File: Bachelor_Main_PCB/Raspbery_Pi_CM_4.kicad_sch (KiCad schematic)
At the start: 10 parts, among them J21 M20-9990245, Q12 NX3008NBKW, Q2 SSM3J358R,LF, U1 SC0683, X1 DF40HC_3.0_-100DS-0.4V_58, X2 DF40HC_3.0_-100DS-0.4V_58

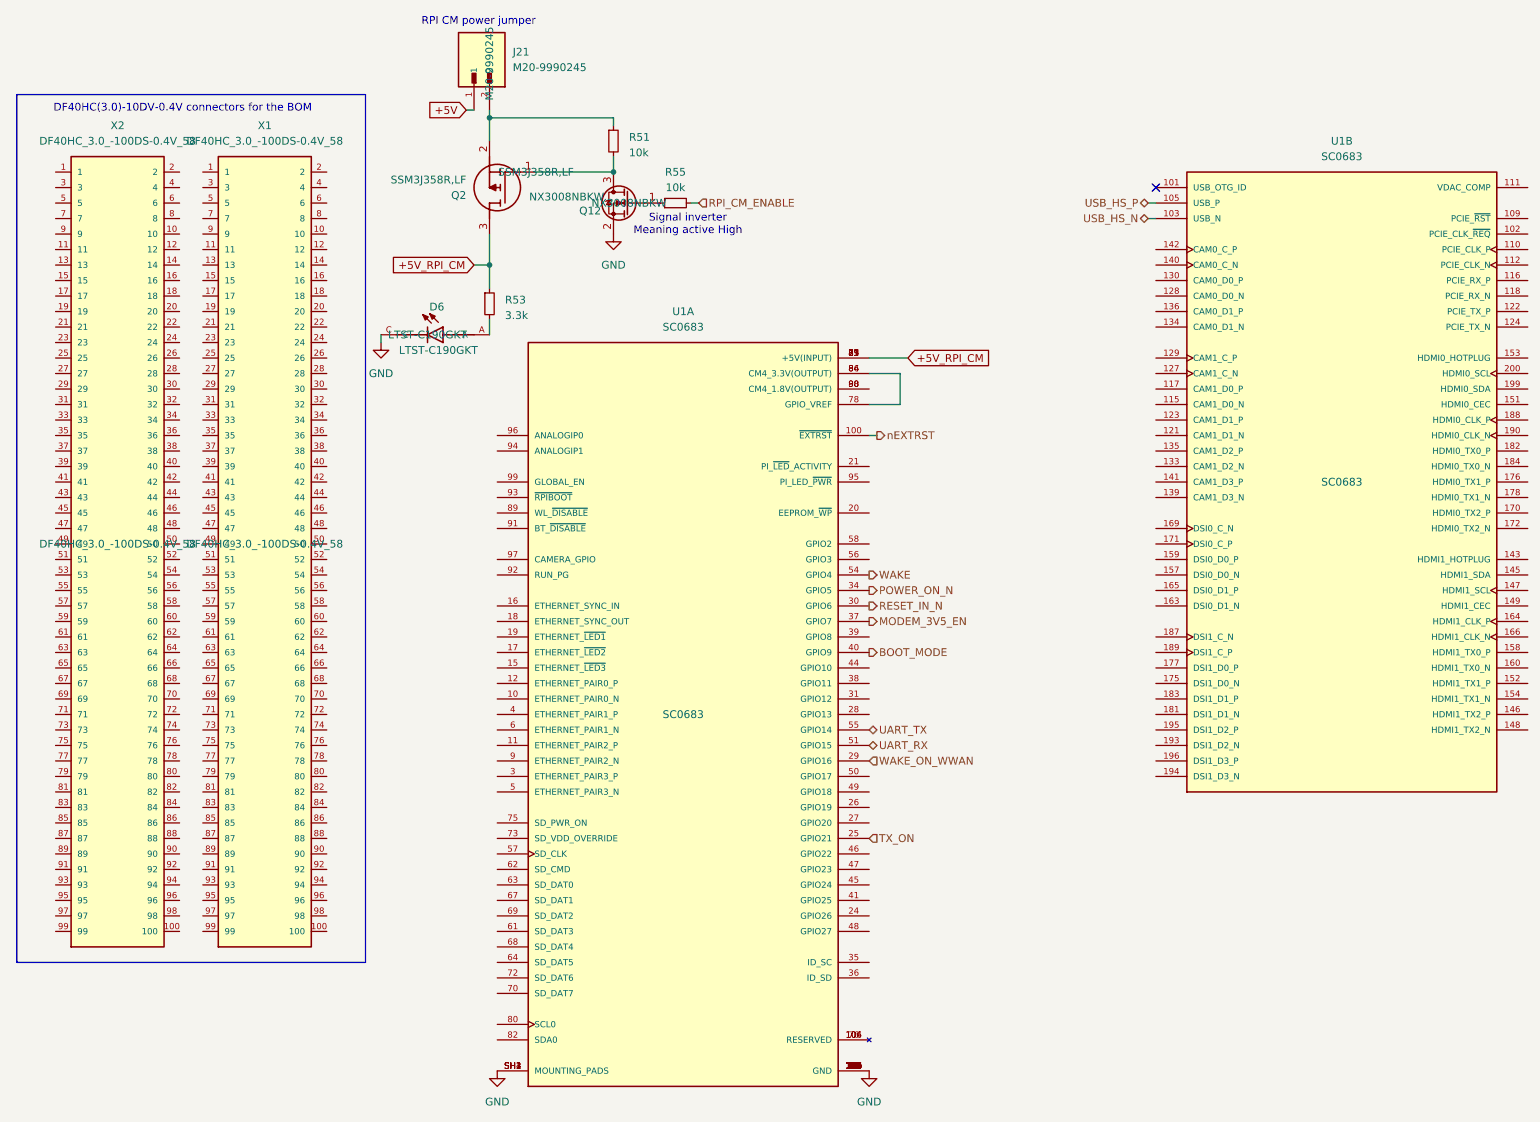
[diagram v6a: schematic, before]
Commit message: Add 1% tolerance field to high tolerance resistors
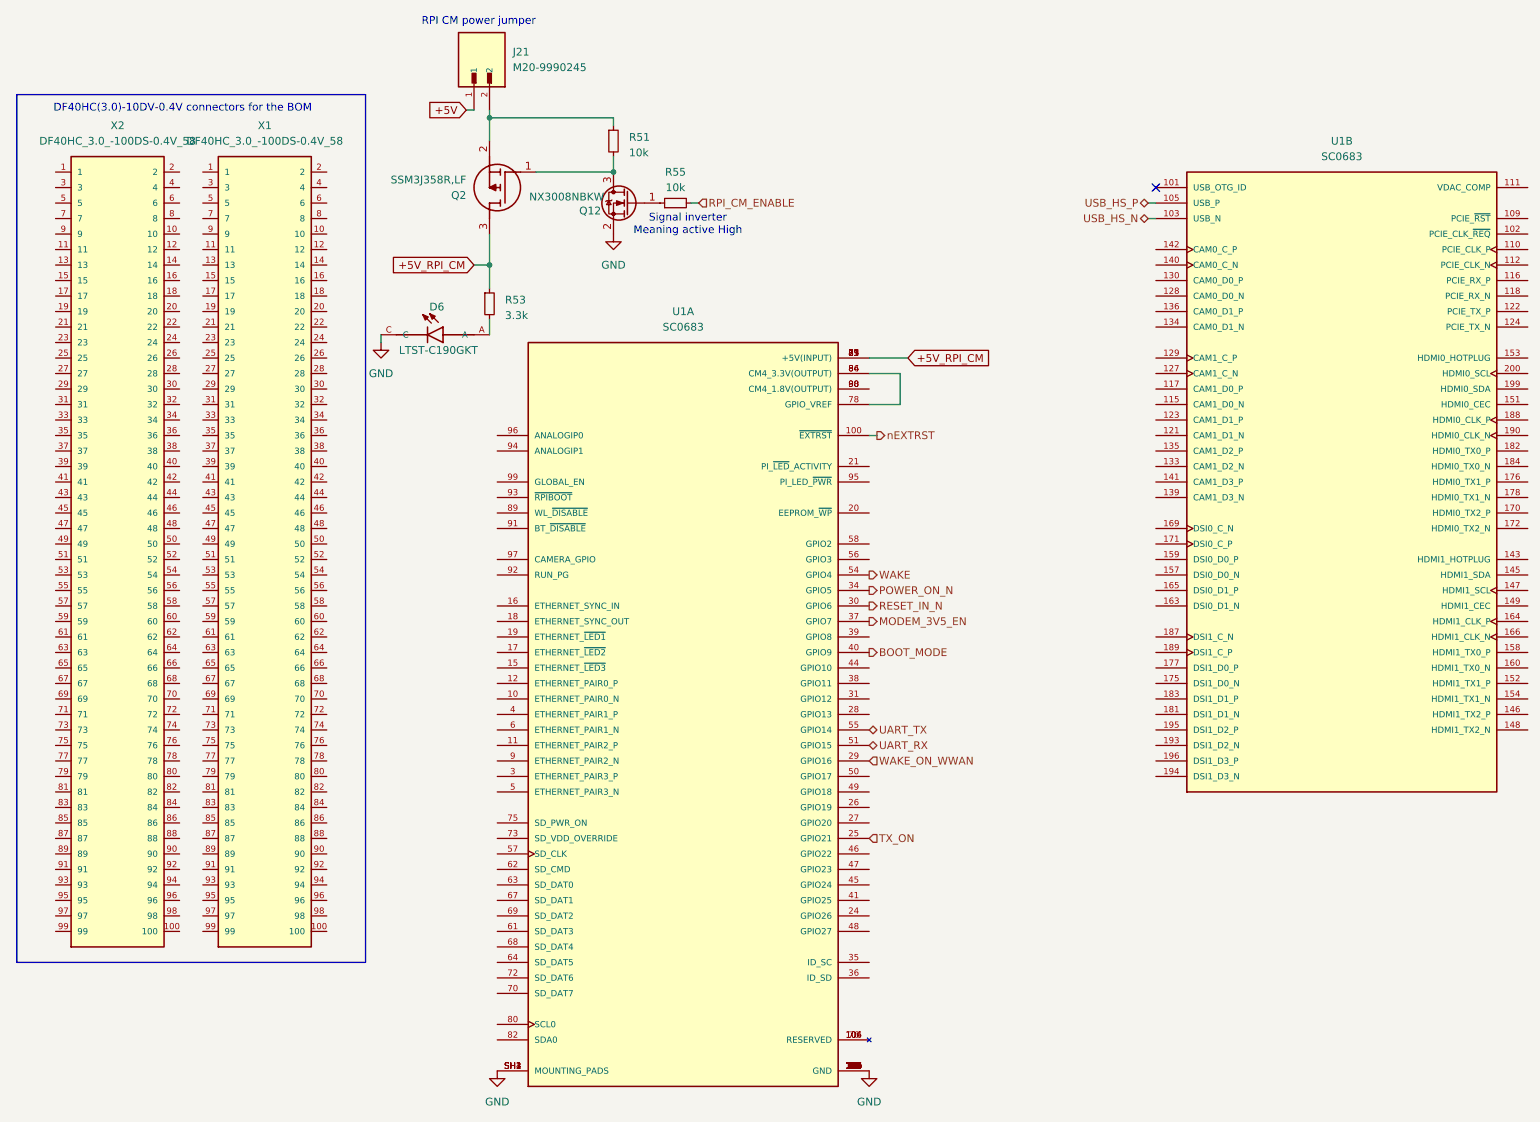
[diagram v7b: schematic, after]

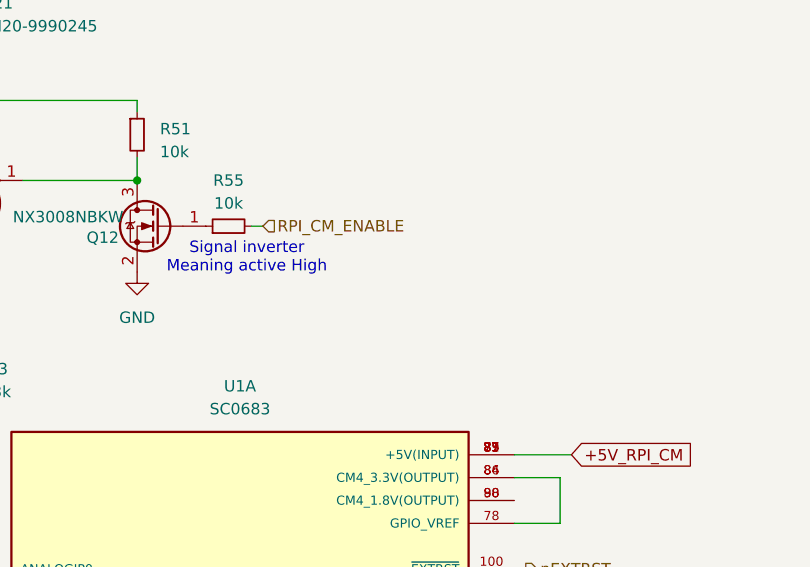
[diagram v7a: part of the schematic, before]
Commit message: Add pulldown to power switch mosfets
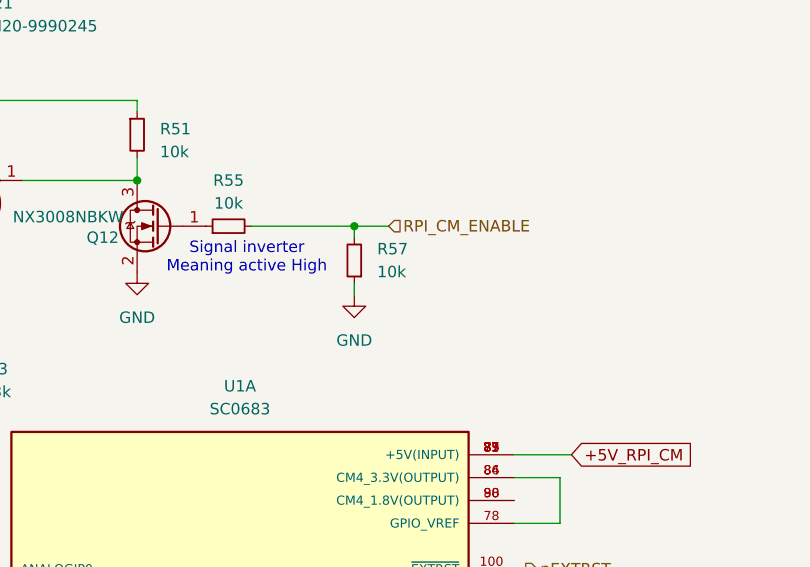
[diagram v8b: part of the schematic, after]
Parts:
- added R57: 10k, Resistor_SMD:R_0603_1608Metric, symbol Device:R_Small
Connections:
- net GND: now also R57.1
- net RPI_CM_ENABLE: now also R57.2
